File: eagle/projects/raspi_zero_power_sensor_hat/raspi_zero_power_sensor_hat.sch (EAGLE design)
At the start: 0 parts

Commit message: modified power entry and boost page
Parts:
- added C1, C10, C3, C4, C9: 22uF, daqcs:CAP_22UF0_0805
- added C11, C2, C5: 100nF, daqcs:CAP_100NF0_0603
- added C6: 2.2uF, daqcs:CAP_2UF2_0603
- added C7: 300pF, daqcs:CAP_300PF0_0603
- added C8: 5.6nF, daqcs:CAP_5NF6_0603
- added J1: JST-PH-2TH-RA, daqcs:JST-PH-2TH-RA_2TH-RA
- added L1: 4.7uH, daqcs:L_4UH7_2SMD
- added R1: 0.075, daqcs:RES_0RS075_0603
- added R2: 7.15k, daqcs:RES_7R15_0603
- added R3: 412k, daqcs:RES_412R0_0603
- added R4, R5: 0, daqcs:RES_0R0_0603
- added R6: 240k, daqcs:RES_240R0_0603
- added R7: 76.8k, daqcs:RES_76R8_0603
- added R8: 820k, daqcs:RES_820R0_0603
- added U2: TPS61089RNRR, daqcs:TPS61089RNRR
- added U3: INA219AIDCNR, daqcs:INA219AIDCNR
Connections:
- new net BOOST_BOOT: C11.1, U2.BOOT
- new net BOOST_COMP: C7.1, R2.2, U2.COMP
- new net BOOST_COMP_RC: C8.1, R2.1
- new net BOOST_FB: R6.1, R7.2, U2.FB
- new net BOOST_FW: R8.1, U2.FSW
- new net BOOST_ILIM: R3.2, U2.ILIM
- new net BOOST_SW: C11.2, L1.2, R8.2, U2.SW
- new net BOOST_VCC: C6.1, U2.EN, U2.VCC
- new net GND: C1.2, C10.2, C2.2, C3.2, C4.2, C5.2, C6.2, C7.2, C8.2, C9.2, J1.2, R3.1, R4.1, R5.1, R7.1, U2.GND, U3.GND
- new net I2C1_RASPI_SCL: U3.SCL
- new net I2C1_RASPI_SDA: U3.SDA
- new net I_MON_A0: R4.2, U3.A0
- new net I_MON_A1: R5.2, U3.A1
- new net PP3V3_RASPI: C2.1, U3.VS
- new net PP5V0_BOOST: C10.1, C9.1, R6.2, U2.VOUT
- new net VBAT: J1.1, R1.1
- new net VBAT_R: C1.1, C3.1, C4.1, C5.1, L1.1, R1.2, U2.VIN
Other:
- note added: "POWER ENTRY AND 5V BOOST"

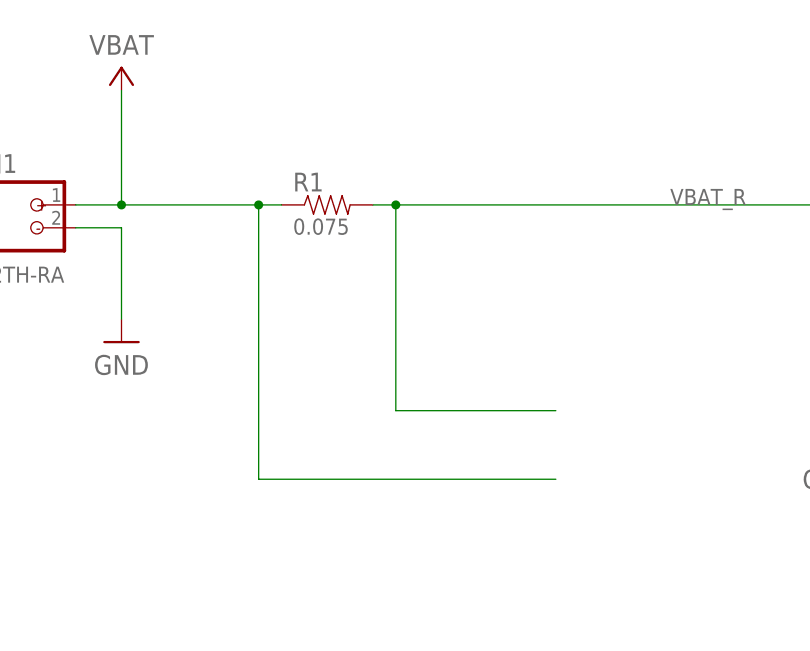
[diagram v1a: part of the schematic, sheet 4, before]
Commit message: added new sense resistor, updated schematic
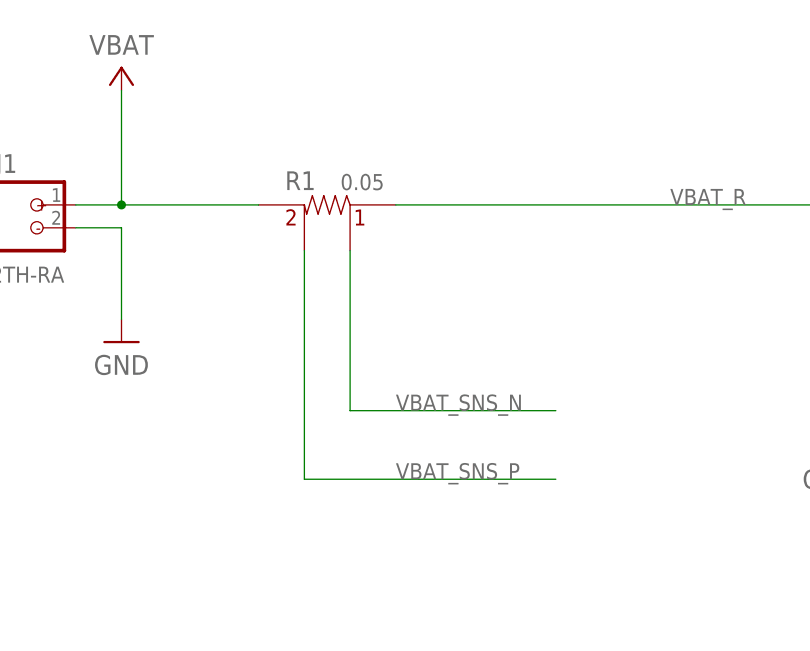
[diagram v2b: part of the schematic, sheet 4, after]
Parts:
- R1: value 0.075 -> 0.05; device daqcs:RES_0RS075_0603 -> daqcs:RES_SNS_0RS050
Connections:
- new net VBAT_SNS_N: R1.1V
- new net VBAT_SNS_P: R1.2V
- net VBAT: now also R1.2A; no longer R1.1
- net VBAT_R: now also R1.1A; no longer R1.2
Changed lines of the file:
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@@
 <part name="FRAME4" library="daqcs" deviceset="FRAME_B_L" device=""/>
 <part name="J1" library="daqcs" deviceset="JST-PH-2" device="_2TH-RA" technology="TH-RA" value="JST-PH-2TH-RA"/>
-<part name="R1" library="daqcs" deviceset="RES" device="_0603" technology="_0RS075" value="0.075"/>
 <part name="GND1" library="daqcs" deviceset="GND" device=""/>
 <part name="U2" library="daqcs" deviceset="TPS61089" device="RNRR" value="TPS61089RNRR"/>
@@
 <part name="C11" library="daqcs" deviceset="CAP" device="_0603" technology="_100NF0" value="100nF"/>
 <part name="R8" library="daqcs" deviceset="RES" device="_0603" technology="_820R0" value="820k"/>
+<part name="R1" library="daqcs" deviceset="RES_SNS" device="" technology="_0RS050" value="0.05"/>
 </parts>
 <sheets>
@@
 <instance part="FRAME4" gate="G$2" x="325.12" y="0"/>
 <instance part="J1" gate="G$1" x="50.8" y="162.56"/>
-<instance part="R1" gate="G$1" x="83.82" y="165.1"/>
 <instance part="GND1" gate="1" x="60.96" y="149.86"/>
 <instance part="U2" gate="A" x="243.84" y="139.7"/>
@@
 </instance>
 <instance part="R8" gate="G$1" x="312.42" y="175.26" rot="R90"/>
+<instance part="R1" gate="G$1" x="83.82" y="165.1" smashed="yes" rot="MR0">
+<attribute name="NAME" x="82.55" y="166.751" size="2.0828" layer="95" rot="MR0"/>
+<attribute name="VALUE" x="90.17" y="166.751" size="1.778" layer="96" rot="MR0"/>
+</instance>
 </instances>
 <busses>
@@
 <net name="VBAT_R" class="0">
 <segment>
-<pinref part="R1" gate="G$1" pin="2"/>
-<wire x1="88.9" y1="165.1" x2="91.44" y2="165.1" width="0.1524" layer="91"/>
-<wire x1="91.44" y1="165.1" x2="91.44" y2="142.24" width="0.1524" layer="91"/>
-<junction x="91.44" y="165.1"/>
 <label x="121.92" y="165.1" size="1.778" layer="95"/>
-<wire x1="91.44" y1="142.24" x2="109.22" y2="142.24" width="0.1524" layer="91"/>
 <pinref part="U2" gate="A" pin="VIN"/>
 <wire x1="91.44" y1="165.1" x2="139.7" y2="165.1" width="0.1524" layer="91"/>
@@
 <wire x1="220.98" y1="193.04" x2="236.22" y2="193.04" width="0.1524" layer="91"/>
 <junction x="220.98" y="165.1"/>
+<pinref part="R1" gate="G$1" pin="1A"/>
 </segment>
 </net>
@@
 <segment>
 <pinref part="J1" gate="G$1" pin="1"/>
-<pinref part="R1" gate="G$1" pin="1"/>
 <wire x1="55.88" y1="165.1" x2="60.96" y2="165.1" width="0.1524" layer="91"/>
 <wire x1="60.96" y1="165.1" x2="76.2" y2="165.1" width="0.1524" layer="91"/>
-<wire x1="76.2" y1="165.1" x2="78.74" y2="165.1" width="0.1524" layer="91"/>
 <wire x1="60.96" y1="165.1" x2="60.96" y2="177.8" width="0.1524" layer="91"/>
 <junction x="60.96" y="165.1"/>
-<wire x1="76.2" y1="165.1" x2="76.2" y2="134.62" width="0.1524" layer="91"/>
-<junction x="76.2" y="165.1"/>
-<wire x1="76.2" y1="134.62" x2="109.22" y2="134.62" width="0.1524" layer="91"/>
 <pinref part="VBAT1" gate="G$1" pin="VBAT"/>
+<pinref part="R1" gate="G$1" pin="2A"/>
 </segment>
 </net>
@@
 </segment>
 </net>
+<net name="VBAT_SNS_P" class="0">
+<segment>
+<wire x1="81.28" y1="134.62" x2="109.22" y2="134.62" width="0.1524" layer="91"/>
+<wire x1="81.28" y1="160.02" x2="81.28" y2="134.62" width="0.1524" layer="91"/>
+<pinref part="R1" gate="G$1" pin="2V"/>
+<label x="91.44" y="134.62" size="1.778" layer="95"/>
+</segment>
+</net>
+<net name="VBAT_SNS_N" class="0">
+<segment>
+<wire x1="86.36" y1="142.24" x2="109.22" y2="142.24" width="0.1524" layer="91"/>
+<wire x1="86.36" y1="160.02" x2="86.36" y2="142.24" width="0.1524" layer="91"/>
+<pinref part="R1" gate="G$1" pin="1V"/>
+<label x="91.44" y="142.24" size="1.778" layer="95"/>
+</segment>
+</net>

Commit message: added battery charget and PMOS fet, plus LEDs and fet driver
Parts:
- added C12: 100nF, daqcs:CAP_100NF0_0603
- added C13: 10uF, daqcs:CAP_10UF0_0603
- added DS1: GREEN, daqcs:LED_G3V2WURTH_0603
- added DS2: YELLOW, daqcs:LED_Y2V0WURTH_0603
- added DS3, DS4: BLUE, daqcs:LED_B3V2WURTH_0603
- added J2: USB_MICROB_RECPT, daqcs:USB_B_MICRO_RIGHT
- added Q1: PMOS-ENHANCE-8A, daqcs:PMOS-1G-1S-4D_PMOS-6P_TSOP-6
- added R10, R11: 2k, daqcs:RES_2R0_0603
- added R12, R13, R14: 1k, daqcs:RES_1R0_0603
- added R15: 0, daqcs:RES_0R0_0603
- added R9: 49.9, daqcs:RES_0R499_0603
- added U1: BUFFER-1-SCHMITT, daqcs:BUFFER-1-SCHMITT_BUF1_TSSOP5
- added U4: MCP73831T, daqcs:MCP73831T-2ATI/OT
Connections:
- new net BOOST_PG: DS3.C, R13.2
- new net BOOST_SW_PG: DS4.C, R14.2
- new net BUFFER_OUT: R9.1, U1.Y
- new net CHG_DONE: DS1.C, R12.2
- new net CHG_ON: DS2.A, R11.2
- new net CHG_PROG: R10.2, U4.PROG
- new net CHG_STAT: DS1.A, DS2.C, U4.STAT
- new net MCU_POWER_OFF: U1.A
- new net PMOS_GATE: Q1.G, R9.2
- new net PP5V0_BOOST_SW: DS4.A, Q1.D@1, Q1.D@2, Q1.D@3, Q1.D@4
- new net PP5V0_USB: C13.1, J2.5V, R11.1, U4.VDD
- new net USB_SHD: J2.SLD, R15.2
- net GND: now also C12.1, C13.2, J2.GND, R10.1, R12.1, R13.1, R14.1, R15.1, U1.GND, U4.VSS
- net PP5V0_BOOST: now also C12.2, DS3.A, Q1.S, U1.VCC
- net VBAT: now also U4.VBAT
- net VBAT_SNS_N: now also U3.VIN-
- net VBAT_SNS_P: now also U3.VIN+
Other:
- note added: "POWER ENTRY, 5V BOOST, AND CHARGER"
- note removed: "POWER ENTRY AND 5V BOOST"
- moved on the sheet: C1, C10, C11, C2, C3, C4, C5, C6, C7, C8, C9, J1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
